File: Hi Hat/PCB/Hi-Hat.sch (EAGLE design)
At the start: 150 parts, among them IC1 LM741P, IC2 LM741P, IC3 LM741P, IC4 LM741P, IC5 LM741P, IC6 LM741P, IC7 LM741P, IC8 LM741P, Q1 2N2222A, Q14 2N3904, Q15 2N3904, Q16 2N3904, Q17 2N3904, Q2 2N2222A, Q3 2N2222A, Q4 2N2222A, Q5 2N2222A, Q6 2N2222A, Q7 2N2222A, Q8 2N2222A, Q9 2N2222A

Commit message: Worked on hi-hat
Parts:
- removed C36, C37, C38, C39, C40, C44, C45, C46: 0.1uF, resistor:C-EU050-024X044
- removed C41: 1.5nF, resistor:C-EU050-024X044
- removed C42, C43: 1nF, resistor:C-EU050-024X044
- removed C47, C49: 2.2u, resistor:C-EU050-024X044
- removed C48: 1u, resistor:C-EU050-024X044
- removed C50: 10uF, rcl:CPOL-USE2.5-6
- removed IC8: LM741P, linear:LM741P
- removed Q10, Q11, Q12, Q13: (no value), Capstone:J176
- removed Q14, Q15, Q16, Q17: 2N3904, transistor:2N3904
- removed Q8, Q9: 2N2222A, SparkFun-DiscreteSemi:TRANS_NPN-P2N2222A
- removed R12, R47, R54: 10k, rcl:R-TRIMM64W
- removed R19, R38, R40, R43, R44, R45, R46, R48, R50, R51, R52, R53, R55, R59, R63, R65, R66, R68: 10k, rcl:R-US_0207/7
- removed R35, R36, R56: 220k, rcl:R-US_0207/7
- removed R37, R69: 47k, rcl:R-US_0207/7
- removed R39, R62: 22k, rcl:R-US_0207/7
- removed R41: 82k, rcl:R-US_0207/7
- removed R42: 560, rcl:R-US_0207/7
- removed R49: 300k, rcl:R-US_0207/7
- removed R57: 470k, rcl:R-US_0207/7
- removed R58: 100k, rcl:R-US_0207/7
- removed R60: 2.7k, rcl:R-US_0207/7
- removed R61, R64: 68k, rcl:R-US_0207/7
- removed R67: 220, rcl:R-US_0207/7
- added J1: (no value), SparkFun-Connectors:CONN_03X2NO_SILK
- added J2: (no value), SparkFun-Connectors:CONN_02
- added TRIM1, TRIM2: 10k, rcl:R-TRIMM64W
- C10: value 0.1uF -> 22nF
- C11: value 0.1uF -> 0.47uF
- C12, C13, C35: value 0.1uF -> 10uF; device resistor:C-EU050-024X044 -> rcl:CPOL-USE2.5-6
- C18, C19: value 47nF -> 0.1uF
- C20, C21: value 33nF -> 0.1uF
- C22: value 0.47uF -> 0.1uF
- C23: value 1nF -> 0.1uF
- C24: value 3.3nF -> 0.1uF
- C26: value 0.1uF -> 1.5nF
- C27: value 3.3nF -> 1nF
- C28: value 22nF -> 1nF
- C32, C34: value 0.1uF -> 2.2u
- C33: value 0.1uF -> 1u
- C5: value 10uF -> 1nF; device rcl:CPOL-USE2.5-6 -> resistor:C-EU050-024X044
- C6: value 0.1uF -> 3.3nF
- C8: value 10uF -> 0.1uF; device rcl:CPOL-USE2.5-6 -> resistor:C-EU050-024X044
- C9: value 10uF -> 3.3nF; device rcl:CPOL-USE2.5-6 -> resistor:C-EU050-024X044
- Q2, Q3, Q4, Q5: value 2N2222A -> (none); device SparkFun-DiscreteSemi:TRANS_NPN-P2N2222A -> Capstone:J176
- Q6, Q7: value 2N2222A -> 2N3904; device SparkFun-DiscreteSemi:TRANS_NPN-P2N2222A -> transistor:2N3904
- R1: value 2k -> 22k
- R11, R13, R16, R18, R28: value 20k -> 10k
- R14: value 10k -> 220k
- R17: device rcl:R-TRIMM64W -> rcl:R-US_0207/7
- R2: value 2k -> 10k
- R21: value 20k -> 300k
- R22: value 10k -> 470k; device rcl:R-TRIMM64W -> rcl:R-US_0207/7
- R23: value 20k -> 100k
- R25: value 10k -> 2.7k
- R26: value 20k -> 68k
- R27: value 10k -> 22k; device rcl:R-TRIMM64W -> rcl:R-US_0207/7
- R29: value 10k -> 68k
- R3: value 680k -> 82k
- R30: value 470k -> 10k
- R31: value 27k -> 10k
- R32: value 22k -> 220
- R33: value 220k -> 10k
- R34: value 220k -> 47k
- R4: value 4.7k -> 560
- R5: value 1k -> 470k
- R6: value 100k -> 27k
- R7: value 68k -> 22k
- R8, R9: value 100k -> 10k
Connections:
- removed net N$11: C14.2, Q1.C, R10.1
- removed net N$12: C14.1, Q2.B, R11.1
- removed net N$13: C15.2, Q1.B, R13.1
- removed net N$15: R11.2, R12.S, R13.2
- removed net N$16: C16.2, Q3.C, R15.1
- removed net N$17: Q14.B, Q15.B
- removed net N$18: C16.1, Q4.B, R16.1
- removed net N$19: C17.2, Q3.B, R18.1
- removed net N$20: C7.1, Q14.E, R3.1
- removed net N$21: C5.-, C6.1, C9.-, R2.1, R5.1, R6.1
- removed net N$22: R33.2, R34.2, R35.2, R36.2, R37.1
- removed net N$23: IC1.-IN, R7.1, R8.2
- removed net N$28: C10.1, R7.2
- removed net N$29: R16.2, R17.S, R18.2
- removed net N$30: C8.+, Q15.C, R4.1
- removed net N$31: C18.2, Q5.C, R20.1
- removed net N$35: C18.1, Q6.B, R21.1
- removed net N$44: C19.2, Q5.B, R23.1
- removed net N$5: C9.+, Q15.E, R5.2
- removed net N$54: R21.2, R22.S, R23.2
- removed net N$55: C20.2, Q7.C, R25.1
- removed net N$56: C20.1, Q8.B, R26.1
- removed net N$57: C21.2, Q7.B, R28.1
- removed net N$58: C23.2, R37.2, R38.2
- removed net N$59: R26.2, R27.S, R28.2
- removed net N$6: C5.+, C6.2, C7.2, R1.1, R3.2, R4.2
- removed net N$9: C13.2, IC1.OUT, R8.1
- removed net OSC1: C15.1, Q2.C, R14.1, R33.1
- removed net OSC2: C17.1, Q4.C, R19.1, R34.1
- removed net OSC3: C19.1, Q6.C, R24.1, R35.1
- removed net OSC4: C21.1, Q8.C, R29.1, R36.1
- removed net POT2B: SV1.7
- removed net SW4: C36.2, IC5.OUT, R53.2
- removed net WHITE_NOISE: C10.2, C8.-, R6.2
- removed net WHITE_NOISE_AMP: C13.1, R43.1, R44.1, R9.1
- removed net WN_SIGNAL: D2.C, D3.A, R58.1
- new net SQ_BUFFERED: C5.2, J1.2, J1.4, J1.6
- new net WN_BUFFERED: J1.1, J1.3, J1.5, R15.1, R16.1
- net +12V: now also C14.2, C17.2, C19.2, C22.2, C24.2, C30.2, C7.2, Q1.C, Q6.C, R30.2, R32.2; no longer C11.2, C25.2, C29.2, C32.2, C34.2, C37.2, C39.2, C45.2, IC8.V+, Q16.C, Q9.C, R1.2, R10.2, R12.E, R14.2, R15.2, R17.E, R19.2, R20.2, R22.E, R24.2, R25.2, R27.E, R29.2, R65.2, R67.2
- net -12V: now also C15.2, C18.2, C20.2, C23.2, C25.2, C31.2, C8.2, R27.1, R31.1, R33.1, TRIM1.S, TRIM2.S; no longer C12.2, C26.2, C30.2, C33.2, C35.2, C38.2, C40.2, C46.2, IC8.V-, R2.2, R47.S, R54.S, R62.1, R66.1, R68.1
- net AGND: now also C12.-, C13.-, C14.1, C15.1, C17.1, C18.1, C19.1, C20.1, C23.1, C24.1, C26.2, C31.1, C33.2, C35.-, C7.1, C8.1, IC3.+IN, IC5.+IN, Q2.G, Q2.S, Q3.S, Q4.G, Q4.S, Q5.S, R10.1, R17.1, R2.1, R26.1, R34.1, R4.1, R5.1, R7.1, SV1.7; no longer C12.1, C26.1, C29.1, C32.1, C33.1, C34.1, C35.1, C37.1, C38.1, C39.1, C40.1, C41.2, C45.1, C46.1, C48.2, C50.-, IC1.+IN, IC4.+IN, IC8.+IN, Q1.E, Q10.G, Q10.S, Q11.S, Q12.G, Q12.S, Q13.S, Q2.E, Q3.E, Q4.E, Q5.E, Q6.E, Q7.E, Q8.E, R30.1, R32.1, R38.1, R40.1, R42.1, R45.1, R52.1, R61.1, R69.1, R9.2
- net BRIDGED_T_OUT: now also C10.1, R8.1, R9.1; no longer C28.1, R50.1, R51.1
- net CYMBAL_PREFILTER: now also C26.1, C27.1, IC6.OUT, R24.2; no longer C41.1, C42.1, IC7.OUT, R59.2
- net CYMBAL_SIGNAL: now also D2.C, D3.A, R22.1; no longer D4.C, D5.A, R57.1
- net FILTER_OUT: now also C29.2, R28.2; no longer C44.2, R63.2
- net N$1: now also C16.2, IC2.OUT, R11.2; no longer C22.2, D1.C, R31.2
- net N$10: now also IC6.-IN, R22.2, R23.2, R24.1; no longer IC7.-IN, R57.2, R58.2, R59.1
- net N$14: now also C6.2, IC1.-IN, R3.1; no longer C24.2, IC2.-IN, R41.1
- net N$2: now also IC2.+IN, Q2.D, R10.2, R9.2; no longer IC5.+IN, Q12.D, R51.2, R52.2
- net N$27: now also C16.1, R13.1; no longer C36.1, R55.1
- net N$3: now also IC2.-IN, Q3.D, R11.1, R8.2; no longer IC5.-IN, Q13.D, R50.2, R53.1
- net N$32: now also IC5.-IN, R20.2, R21.1; no longer IC4.-IN, R48.2, R49.1
- net N$33: now also IC7.-IN, R28.1, R29.2; no longer IC8.-IN, R63.1, R64.2
- net N$34: now also C21.1, R20.1; no longer C31.1, R48.1
- net N$36: now also C21.2, IC4.OUT, R18.2; no longer C31.2, IC3.OUT, R46.2
- net N$38: now also D4.A, D5.C, IC5.OUT, R21.2; no longer D2.A, D3.C, IC4.OUT, R49.2
- net N$39: now also D2.A, D3.C, IC3.OUT, R14.2; no longer D4.A, D5.C, IC6.OUT, R56.2
- net N$4: now also IC2.ON2, TRIM1.A; no longer IC5.ON2, R54.A
- net N$47: now also C6.1, C9.2, R4.2; no longer C24.1, C27.2, R42.2
- net N$60: now also C10.2, C9.1, IC1.OUT, R3.2; no longer C27.1, C28.2, IC2.OUT, R41.2
- net N$61: now also IC1.+IN, R1.2, R2.2; no longer IC2.+IN, R39.2, R40.2
- net N$62: now also C5.1, R1.1; no longer C23.1, R39.1
- net N$63: now also C32.1, Q7.B, R30.1, R31.2; no longer C47.1, Q17.B, R65.1, R66.2
- net N$64: now also Q1.E, R5.2; no longer Q9.E, R30.2
- net N$65: now also IC4.+IN, Q4.D, R16.2, R17.2; no longer IC3.+IN, Q10.D, R44.2, R45.2
- net N$66: now also IC4.-IN, Q5.D, R15.2, R18.1; no longer IC3.-IN, Q11.D, R43.2, R46.1
- net N$67: now also IC4.ON2, TRIM2.A; no longer IC3.ON2, R47.A
- net N$68: now also IC4.ON1, TRIM2.E; no longer IC3.ON1, R47.E
- net N$7: now also IC2.ON1, TRIM1.E; no longer IC5.ON1, R54.E
- net N$71: now also C34.1, Q7.E, R33.2; no longer C49.1, Q17.E, R68.2
- net N$72: now also C33.1, C35.+, Q7.C, R32.1; no longer C48.1, C50.+, Q17.C, R67.1
- net N$73: now also C27.2, C28.1, R25.2; no longer C42.2, C43.1, R60.2
- net N$74: now also C28.2, Q6.B, R26.2; no longer C43.2, Q16.B, R61.2
- net N$75: now also C29.1, Q6.E, R25.1, R27.2; no longer C44.1, Q16.E, R60.1, R62.2
- net N$8: now also IC3.-IN, R13.2, R14.1; no longer IC6.-IN, R55.2, R56.1
- net OUTPUT: now also C34.2, R34.2; no longer C49.2, R69.2
- net POT1A: now also D4.C, D5.A, J2.1
- net POT1B: now also J2.2, R23.1
- net POT2A: now also C11.2, C12.+, C13.+, D1.C, R6.2
- net PRE_CC: now also C32.2, IC7.OUT, R29.1; no longer C47.2, IC8.OUT, R64.1
- net TRIGGER: now also Q1.B; no longer Q9.B
- net VCA_TRIGGER: now also Q3.G, Q5.G, R6.1, R7.2; no longer Q11.G, Q13.G, R31.1, R32.2
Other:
- note added: "Note: POT2B is grounded to AGND"
- note added: "Note: Short Jumper for open hi-hat Third pin of POT1 should be grounded"
- note removed: "1136 Hz Oscillator Trimpot should be around 2.19k"
- note removed: "305 Hz Oscillator Trimpot should be around 3.91k"
- note removed: "444 Hz Oscillator Trimpot should be around 550 ohms"
- note removed: "794 Hz Oscillator Trimpot should be around 2.05k"
- note removed: "White Noise Amplifier"
- note removed: "White Noise Generator"
- moved on the sheet: C1, C10, C11, C14, C15, C16, C17, C18, C19, C2, C20, C21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

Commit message: Made more progress on hi-hat
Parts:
- removed C35: 10uF, rcl:CPOL-USE2.5-6
- added R35: 47k, rcl:R-US_0207/7
- C13: value 10uF -> 0.1uF; device rcl:CPOL-USE2.5-6 -> resistor:C-EU050-024X044
- C25: value 0.1uF -> 1.5nF
- C26: value 1.5nF -> 1nF
- C28: value 1nF -> 0.1uF
- C31: value 0.1uF -> 2.2u
- C32: value 2.2u -> 1u
- C33: value 1u -> 2.2u
- C34: value 2.2u -> 10uF; device resistor:C-EU050-024X044 -> rcl:CPOL-USE2.5-6
- R27: value 22k -> 0
- R28: value 10k -> 22k
- R29: value 68k -> 10k
- R30: value 10k -> 68k
- R32: value 220 -> 10k
- R33: value 10k -> 220
- R34: value 47k -> 10k
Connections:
- new net N$5: Q6.C, R27.2
- net +12V: now also C13.2, C16.2, C18.2, C21.2, C23.2, C29.2, R27.1, R31.2, R33.2; no longer C14.2, C17.2, C19.2, C22.2, C24.2, C30.2, Q6.C, R30.2, R32.2
- net -12V: now also C14.2, C17.2, C19.2, C22.2, C24.2, C30.2, R28.1, R32.1, R34.1; no longer C15.2, C18.2, C20.2, C23.2, C25.2, C31.2, R27.1, R31.1, R33.1
- net AGND: now also C13.1, C16.1, C21.1, C25.2, C29.1, C32.2, C34.-, R35.1; no longer C13.-, C15.1, C20.1, C25.1, C26.2, C31.1, C33.2, C35.-, R34.1
- net CYMBAL_PREFILTER: now also C25.1; no longer C27.1
- net FILTER_OUT: now also C28.2, R29.2; no longer C29.2, R28.2
- net N$1: now also C15.2; no longer C16.2
- net N$27: now also C15.1; no longer C16.1
- net N$33: now also R29.1, R30.2; no longer R28.1, R29.2
- net N$34: now also C20.1; no longer C21.1
- net N$36: now also C20.2; no longer C21.2
- net N$63: now also C31.1, R31.1, R32.2; no longer C32.1, R30.1, R31.2
- net N$71: now also C33.1, R34.2; no longer C34.1, R33.2
- net N$72: now also C32.1, C34.+, R33.1; no longer C33.1, C35.+, R32.1
- net N$73: now also C26.2, C27.1; no longer C27.2, C28.1
- net N$74: now also C27.2; no longer C28.2
- net N$75: now also C28.1, R28.2; no longer C29.1, R27.2
- net OUTPUT: now also C33.2, R35.2; no longer C34.2, R34.2
- net POT2A: no longer C13.+
- net PRE_CC: now also C31.2, R30.1; no longer C32.2, R29.1
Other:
- note added: "Note: Resistor at the collector should be a jumper. The resistor is only there so biasing can be changed if needed."
- moved on the sheet: C14, C15, C16, C17, C18, C19, C20, C21, C22, C23, C24, C25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

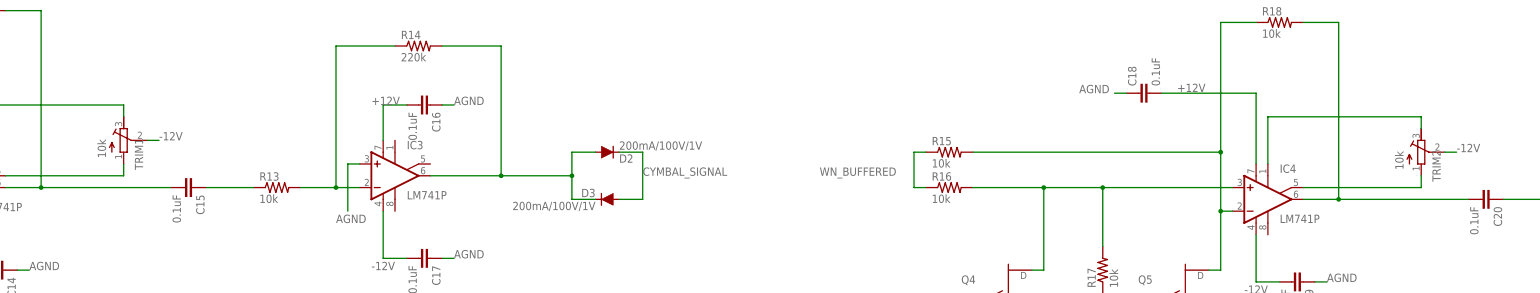
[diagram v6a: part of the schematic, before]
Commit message: Worked on Hi-hat and waveform generator board
Changed trimpots to the proper part. Added test points to the waveform generator board and fixed silkscreen, ran DRC.
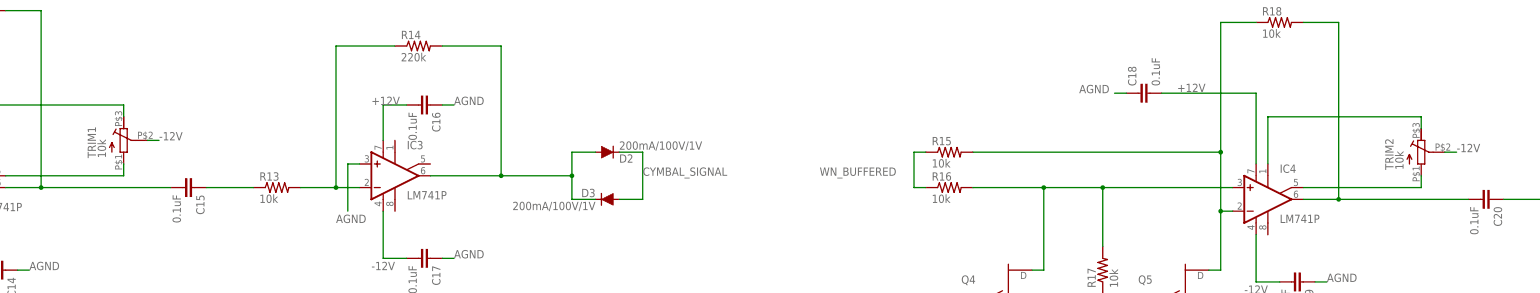
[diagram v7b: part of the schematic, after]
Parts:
- TRIM1, TRIM2: device rcl:R-TRIMM64W -> Capstone:10K_TRIMMER
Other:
- moved on the sheet: TRIM1, TRIM2
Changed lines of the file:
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@@
 <part name="C19" library="resistor" library_urn="urn:adsk.eagle:library:348" deviceset="C-EU" device="050-024X044" package3d_urn="urn:adsk.eagle:package:26162/1" value="0.1uF"/>
 <part name="C18" library="resistor" library_urn="urn:adsk.eagle:library:348" deviceset="C-EU" device="050-024X044" package3d_urn="urn:adsk.eagle:package:26162/1" value="0.1uF"/>
-<part name="TRIM2" library="rcl" library_urn="urn:adsk.eagle:library:334" deviceset="R-TRIMM" device="64W" package3d_urn="urn:adsk.eagle:package:23748/1" value="10k"/>
 <part name="Q5" library="Capstone" deviceset="J176" device=""/>
 <part name="C10" library="resistor" library_urn="urn:adsk.eagle:library:348" deviceset="C-EU" device="050-024X044" package3d_urn="urn:adsk.eagle:package:26162/1" value="22nF"/>
@@
 <part name="C14" library="resistor" library_urn="urn:adsk.eagle:library:348" deviceset="C-EU" device="050-024X044" package3d_urn="urn:adsk.eagle:package:26162/1" value="0.1uF"/>
 <part name="C13" library="resistor" library_urn="urn:adsk.eagle:library:348" deviceset="C-EU" device="050-024X044" package3d_urn="urn:adsk.eagle:package:26162/1" value="0.1uF"/>
-<part name="TRIM1" library="rcl" library_urn="urn:adsk.eagle:library:334" deviceset="R-TRIMM" device="64W" package3d_urn="urn:adsk.eagle:package:23748/1" value="10k"/>
 <part name="Q3" library="Capstone" deviceset="J176" device=""/>
 <part name="R8" library="rcl" library_urn="urn:adsk.eagle:library:334" deviceset="R-US_" device="0207/7" package3d_urn="urn:adsk.eagle:package:23493/1" value="10k"/>
@@
 <part name="C12" library="rcl" library_urn="urn:adsk.eagle:library:334" deviceset="CPOL-US" device="E2.5-6" package3d_urn="urn:adsk.eagle:package:23349/1" value="10uF"/>
 <part name="R27" library="rcl" library_urn="urn:adsk.eagle:library:334" deviceset="R-US_" device="0207/7" package3d_urn="urn:adsk.eagle:package:23493/1" value="0"/>
+<part name="TRIM1" library="Capstone" deviceset="10K_TRIMMER" device="" value="10k"/>
+<part name="TRIM2" library="Capstone" deviceset="10K_TRIMMER" device="" value="10k"/>
 </parts>
 <sheets>
@@
 <attribute name="VALUE" x="1162.939" y="377.444" size="1.778" layer="96" rot="R90"/>
 </instance>
-<instance part="TRIM2" gate="G$1" x="1219.2" y="363.22" smashed="yes">
-<attribute name="NAME" x="1223.391" y="356.87" size="1.778" layer="95" rot="R90"/>
-<attribute name="VALUE" x="1215.39" y="359.41" size="1.778" layer="96" rot="R90"/>
-</instance>
 <instance part="Q5" gate="G$1" x="1168.4" y="335.28" smashed="yes" rot="MR180">
 <attribute name="NAME" x="1158.24" y="336.677" size="1.778" layer="95" rot="MR180"/>
@@
 <attribute name="VALUE" x="883.539" y="379.984" size="1.778" layer="96" rot="R90"/>
 </instance>
-<instance part="TRIM1" gate="G$1" x="939.8" y="365.76" smashed="yes">
-<attribute name="NAME" x="943.991" y="359.41" size="1.778" layer="95" rot="R90"/>
-<attribute name="VALUE" x="935.99" y="361.95" size="1.778" layer="96" rot="R90"/>
-</instance>
 <instance part="Q3" gate="G$1" x="889" y="337.82" smashed="yes" rot="MR180">
 <attribute name="NAME" x="878.84" y="339.217" size="1.778" layer="95" rot="MR180"/>
@@
 <attribute name="NAME" x="1660.1186" y="379.73" size="1.778" layer="95" rot="R270"/>
 <attribute name="VALUE" x="1655.318" y="379.73" size="1.778" layer="96" rot="R270"/>
+</instance>
+<instance part="TRIM1" gate="G$1" x="939.8" y="365.76" smashed="yes">
+<attribute name="NAME" x="933.831" y="361.95" size="1.778" layer="95" rot="R90"/>
+<attribute name="VALUE" x="935.99" y="361.95" size="1.778" layer="96" rot="R90"/>
+</instance>
+<instance part="TRIM2" gate="G$1" x="1219.2" y="363.22" smashed="yes">
+<attribute name="NAME" x="1213.231" y="359.41" size="1.778" layer="95" rot="R90"/>
+<attribute name="VALUE" x="1215.39" y="359.41" size="1.778" layer="96" rot="R90"/>
 </instance>
 </instances>
@@
 </segment>
 <segment>
-<pinref part="TRIM2" gate="G$1" pin="S"/>
 <wire x1="1224.28" y1="363.22" x2="1226.82" y2="363.22" width="0.1524" layer="91"/>
 <label x="1226.82" y="363.22" size="1.778" layer="95"/>
+<pinref part="TRIM2" gate="G$1" pin="S"/>
 </segment>
 <segment>
@@
 </segment>
 <segment>
-<pinref part="TRIM1" gate="G$1" pin="S"/>
 <wire x1="944.88" y1="365.76" x2="947.42" y2="365.76" width="0.1524" layer="91"/>
 <label x="947.42" y="365.76" size="1.778" layer="95"/>
+<pinref part="TRIM1" gate="G$1" pin="S"/>
 </segment>
 <segment>
@@
 <segment>
 <pinref part="IC4" gate="A" pin="ON2"/>
-<pinref part="TRIM2" gate="G$1" pin="A"/>
 <wire x1="1193.8" y1="355.6" x2="1219.2" y2="355.6" width="0.1524" layer="91"/>
 <wire x1="1219.2" y1="355.6" x2="1219.2" y2="358.14" width="0.1524" layer="91"/>
+<pinref part="TRIM2" gate="G$1" pin="A"/>
 </segment>
 </net>
@@
 <wire x1="1186.18" y1="360.68" x2="1186.18" y2="370.84" width="0.1524" layer="91"/>
 <wire x1="1186.18" y1="370.84" x2="1219.2" y2="370.84" width="0.1524" layer="91"/>
+<wire x1="1219.2" y1="370.84" x2="1219.2" y2="368.3" width="0.1524" layer="91"/>
 <pinref part="TRIM2" gate="G$1" pin="E"/>
-<wire x1="1219.2" y1="370.84" x2="1219.2" y2="368.3" width="0.1524" layer="91"/>
 </segment>
 </net>
@@
 <segment>
 <pinref part="IC2" gate="A" pin="ON2"/>
-<pinref part="TRIM1" gate="G$1" pin="A"/>
 <wire x1="914.4" y1="358.14" x2="939.8" y2="358.14" width="0.1524" layer="91"/>
 <wire x1="939.8" y1="358.14" x2="939.8" y2="360.68" width="0.1524" layer="91"/>
+<pinref part="TRIM1" gate="G$1" pin="A"/>
 </segment>
 </net>
@@
 <wire x1="906.78" y1="363.22" x2="906.78" y2="373.38" width="0.1524" layer="91"/>
 <wire x1="906.78" y1="373.38" x2="939.8" y2="373.38" width="0.1524" layer="91"/>
+<wire x1="939.8" y1="373.38" x2="939.8" y2="370.84" width="0.1524" layer="91"/>
 <pinref part="TRIM1" gate="G$1" pin="E"/>
-<wire x1="939.8" y1="373.38" x2="939.8" y2="370.84" width="0.1524" layer="91"/>
-</segment>
-</net>
+</segment>
+</net>

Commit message: Worked more on cymbals
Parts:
- added R12: 22k, rcl:R-US_0207/7
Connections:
- new net N$6: C11.2, C12.+, D1.C, R12.2, R6.2
- net POT2A: now also R12.1; no longer C11.2, C12.+, D1.C, R6.2
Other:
- moved on the sheet: R6, R7
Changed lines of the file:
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@@
 <part name="TRIM1" library="Capstone" deviceset="10K_TRIMMER" device="" value="10k"/>
 <part name="TRIM2" library="Capstone" deviceset="10K_TRIMMER" device="" value="10k"/>
+<part name="R12" library="rcl" library_urn="urn:adsk.eagle:library:334" deviceset="R-US_" device="0207/7" package3d_urn="urn:adsk.eagle:package:23493/1" value="22k"/>
 </parts>
 <sheets>
@@
 <attribute name="VALUE" x="1661.922" y="334.01" size="1.778" layer="96" rot="R90"/>
 </instance>
-<instance part="R6" gate="G$1" x="693.42" y="358.14" smashed="yes" rot="R90">
-<attribute name="NAME" x="691.9214" y="354.33" size="1.778" layer="95" rot="R90"/>
-<attribute name="VALUE" x="696.722" y="354.33" size="1.778" layer="96" rot="R90"/>
-</instance>
-<instance part="R7" gate="G$1" x="693.42" y="342.9" smashed="yes" rot="R90">
-<attribute name="NAME" x="691.9214" y="339.09" size="1.778" layer="95" rot="R90"/>
-<attribute name="VALUE" x="696.722" y="339.09" size="1.778" layer="96" rot="R90"/>
+<instance part="R6" gate="G$1" x="706.12" y="358.14" smashed="yes" rot="R90">
+<attribute name="NAME" x="704.6214" y="354.33" size="1.778" layer="95" rot="R90"/>
+<attribute name="VALUE" x="709.422" y="354.33" size="1.778" layer="96" rot="R90"/>
+</instance>
+<instance part="R7" gate="G$1" x="706.12" y="342.9" smashed="yes" rot="R90">
+<attribute name="NAME" x="704.6214" y="339.09" size="1.778" layer="95" rot="R90"/>
+<attribute name="VALUE" x="709.422" y="339.09" size="1.778" layer="96" rot="R90"/>
 </instance>
 <instance part="R5" gate="G$1" x="640.08" y="347.98" smashed="yes" rot="R90">
@@
 <attribute name="NAME" x="1213.231" y="359.41" size="1.778" layer="95" rot="R90"/>
 <attribute name="VALUE" x="1215.39" y="359.41" size="1.778" layer="96" rot="R90"/>
+</instance>
+<instance part="R12" gate="G$1" x="693.42" y="355.6" smashed="yes" rot="R90">
+<attribute name="NAME" x="691.9214" y="351.79" size="1.778" layer="95" rot="R90"/>
+<attribute name="VALUE" x="696.722" y="351.79" size="1.778" layer="96" rot="R90"/>
 </instance>
 </instances>
@@
 </segment>
 <segment>
-<pinref part="D1" gate="G$1" pin="C"/>
-<wire x1="652.78" y1="365.76" x2="662.94" y2="365.76" width="0.1524" layer="91"/>
-<pinref part="R6" gate="G$1" pin="2"/>
-<wire x1="662.94" y1="365.76" x2="678.18" y2="365.76" width="0.1524" layer="91"/>
-<wire x1="678.18" y1="365.76" x2="693.42" y2="365.76" width="0.1524" layer="91"/>
-<wire x1="693.42" y1="365.76" x2="693.42" y2="363.22" width="0.1524" layer="91"/>
-<pinref part="C11" gate="G$1" pin="2"/>
-<wire x1="662.94" y1="353.06" x2="662.94" y2="365.76" width="0.1524" layer="91"/>
-<junction x="662.94" y="365.76"/>
-<pinref part="C12" gate="G$1" pin="+"/>
-<wire x1="678.18" y1="353.06" x2="678.18" y2="365.76" width="0.1524" layer="91"/>
-<junction x="678.18" y="365.76"/>
-<label x="685.8" y="365.76" size="1.778" layer="95"/>
+<pinref part="R12" gate="G$1" pin="1"/>
+<wire x1="693.42" y1="350.52" x2="693.42" y2="347.98" width="0.1524" layer="91"/>
+<label x="690.88" y="345.44" size="1.778" layer="95"/>
 </segment>
 </net>
@@
 <wire x1="662.94" y1="332.74" x2="662.94" y2="345.44" width="0.1524" layer="91"/>
 <label x="657.86" y="330.2" size="1.778" layer="95" rot="MR0"/>
-<wire x1="693.42" y1="337.82" x2="693.42" y2="332.74" width="0.1524" layer="91"/>
-<wire x1="693.42" y1="332.74" x2="678.18" y2="332.74" width="0.1524" layer="91"/>
+<wire x1="706.12" y1="337.82" x2="706.12" y2="332.74" width="0.1524" layer="91"/>
+<wire x1="706.12" y1="332.74" x2="678.18" y2="332.74" width="0.1524" layer="91"/>
 <junction x="662.94" y="332.74"/>
 <pinref part="R7" gate="G$1" pin="1"/>
@@
 </segment>
 <segment>
-<wire x1="693.42" y1="353.06" x2="693.42" y2="350.52" width="0.1524" layer="91"/>
+<wire x1="706.12" y1="353.06" x2="706.12" y2="350.52" width="0.1524" layer="91"/>
 <pinref part="R6" gate="G$1" pin="1"/>
 <pinref part="R7" gate="G$1" pin="2"/>
-<wire x1="693.42" y1="350.52" x2="693.42" y2="347.98" width="0.1524" layer="91"/>
-<wire x1="693.42" y1="350.52" x2="701.04" y2="350.52" width="0.1524" layer="91"/>
-<junction x="693.42" y="350.52"/>
-<label x="701.04" y="350.52" size="1.778" layer="95"/>
+<wire x1="706.12" y1="350.52" x2="706.12" y2="347.98" width="0.1524" layer="91"/>
+<wire x1="706.12" y1="350.52" x2="711.2" y2="350.52" width="0.1524" layer="91"/>
+<junction x="706.12" y="350.52"/>
+<label x="713.74" y="350.52" size="1.778" layer="95"/>
 </segment>
 <segment>
@@
 </segment>
 </net>
+<net name="N$6" class="0">
+<segment>
+<pinref part="D1" gate="G$1" pin="C"/>
+<pinref part="R6" gate="G$1" pin="2"/>
+<wire x1="652.78" y1="365.76" x2="662.94" y2="365.76" width="0.1524" layer="91"/>
+<wire x1="662.94" y1="365.76" x2="678.18" y2="365.76" width="0.1524" layer="91"/>
+<wire x1="678.18" y1="365.76" x2="693.42" y2="365.76" width="0.1524" layer="91"/>
+<wire x1="693.42" y1="365.76" x2="706.12" y2="365.76" width="0.1524" layer="91"/>
+<wire x1="706.12" y1="365.76" x2="706.12" y2="363.22" width="0.1524" layer="91"/>
+<pinref part="R12" gate="G$1" pin="2"/>
+<wire x1="693.42" y1="360.68" x2="693.42" y2="365.76" width="0.1524" layer="91"/>
+<junction x="693.42" y="365.76"/>
+<pinref part="C12" gate="G$1" pin="+"/>
+<wire x1="678.18" y1="353.06" x2="678.18" y2="365.76" width="0.1524" layer="91"/>
+<junction x="678.18" y="365.76"/>
+<pinref part="C11" gate="G$1" pin="2"/>
+<wire x1="662.94" y1="353.06" x2="662.94" y2="365.76" width="0.1524" layer="91"/>
+<junction x="662.94" y="365.76"/>
+</segment>
+</net>
